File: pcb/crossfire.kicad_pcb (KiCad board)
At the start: 4 copper layers, 100 x 49.8 mm, 104 parts, among them J1 USB-C, J2 SWD+UART, J3 USB_A, J4 USB_A, J5 USB_A, J6 USB_A, SW1 BOOT, SW2 RESET, SW3 USER, U1 USBLC6-2SC6, U10 TPS2065C, U11 USBLC6-2SC6, U12 TPS2065C, U13 USBLC6-2SC6, U2 W25Q128JVS, U3 RP2350A, U4 AP63203WU, U5 USB2514B, U6 TPS2065C, U7 USBLC6-2SC6, U8 TPS2065C, U9 USBLC6-2SC6, Y1 12MHz, Y2 24MHz

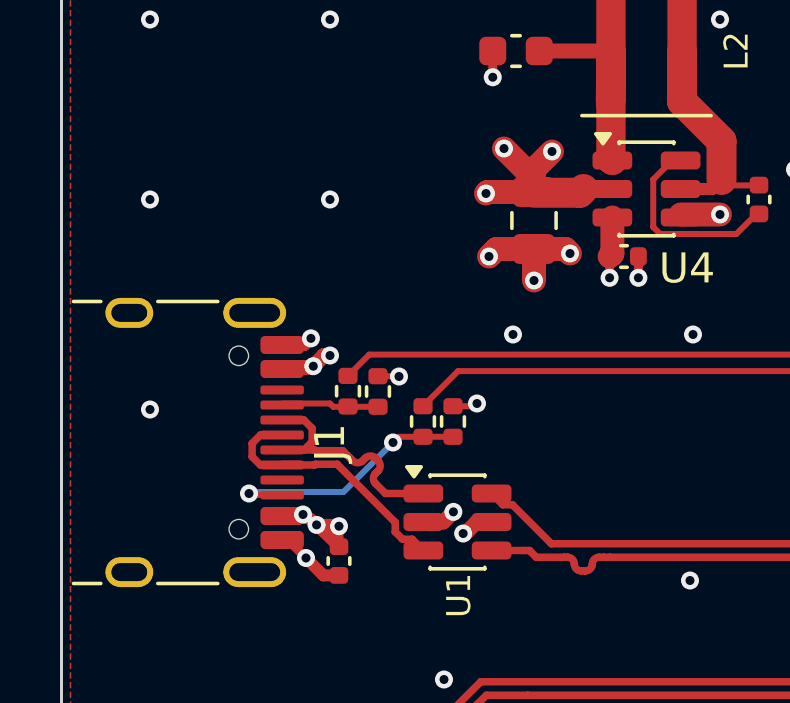
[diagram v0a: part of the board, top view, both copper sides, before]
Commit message: a resettable fuse on the 5 V input
F1, a 1812 polymer fuse with a 2.6 A hold and a 5 A trip, goes in series with VBUS at the
receptacle, ahead of everything. The wire between the receptacle's four VBUS pins and the fuse is
its own net, VBUS_IN, in the heavy-copper class; everything after the fuse is +5V as before. On the
board the fuse sits 5 mm from the receptacle in a spot checked clear of every other net's copper,
with its pads on the two nets and the receptacle's VBUS pads moved to the new one. The copper from
those pads through the fuse to the 5 V vias is the next hand edit; until it is drawn the rules
check lists the old VBUS tracks as shorting the two nets. The design document says why a
resettable part and what it costs.

Co-Authored-By: Claude Fable 5.1 <noreply@anthropic.com>
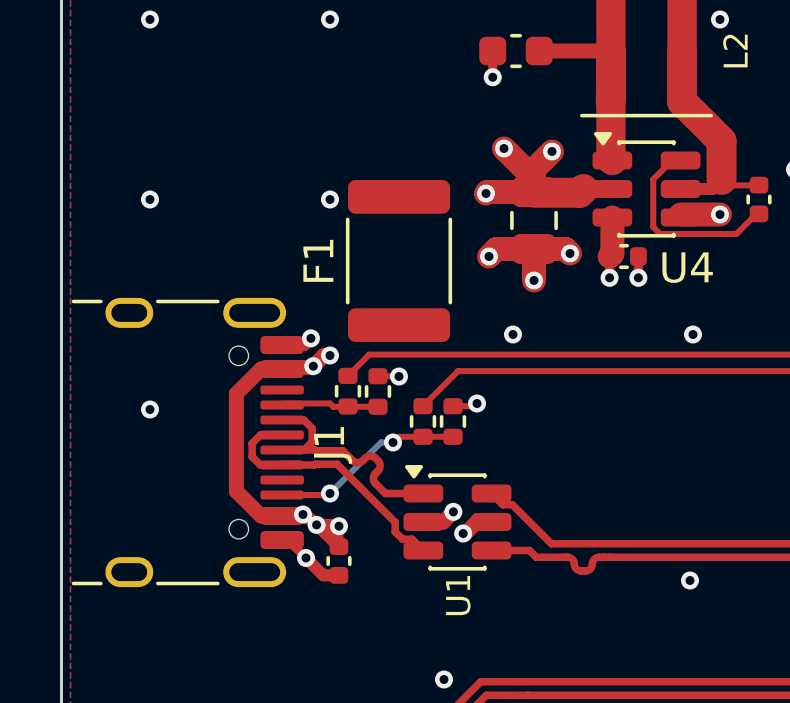
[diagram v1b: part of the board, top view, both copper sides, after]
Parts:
- added F1: 2.6A, Fuse:Fuse_1812_4532Metric, F.Cu at (109.8, 62.0)
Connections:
- J1 pad A4: +5V -> /upstream_data/VBUS_IN
- J1 pad A9: +5V -> /upstream_data/VBUS_IN
- J1 pad B4: +5V -> /upstream_data/VBUS_IN
- J1 pad B9: +5V -> /upstream_data/VBUS_IN
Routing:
- net +5V: track 34.7 -> 41.6 mm
- net /upstream_data/CC2: track 8.71 -> 6.50 mm

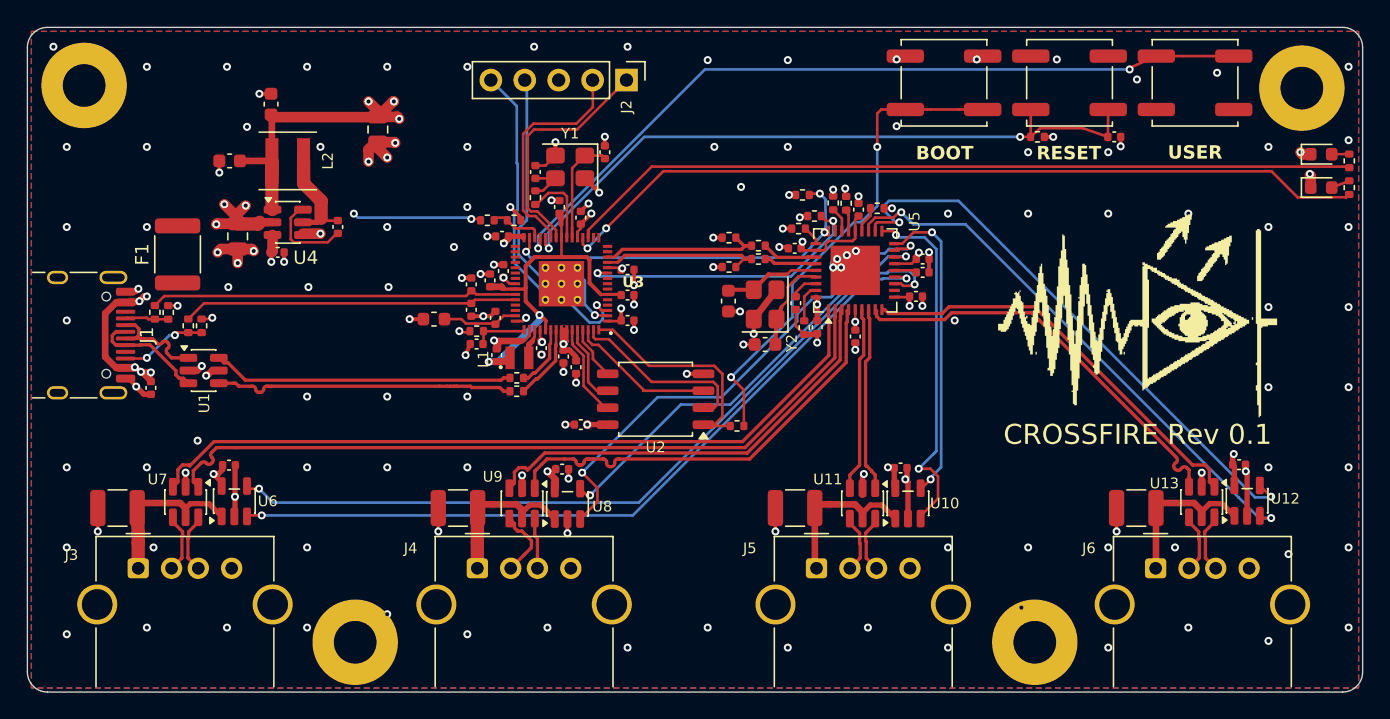
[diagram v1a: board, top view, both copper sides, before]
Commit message: board: VBUS routed through the fuse; the export names the fuse's package plainly
The receptacle's VBUS pads reach the fuse on their own net and the fuse feeds the 5 V plane; the
rules check is clean with parity and a fresh fill. The bill's footprint column now reduces a fuse
footprint's two-size name to its imperial code, as it already did for the chip parts, so the
fabricator's parser reads 1812 and not the metric 4532.

Co-Authored-By: Claude Fable 5.1 <noreply@anthropic.com>
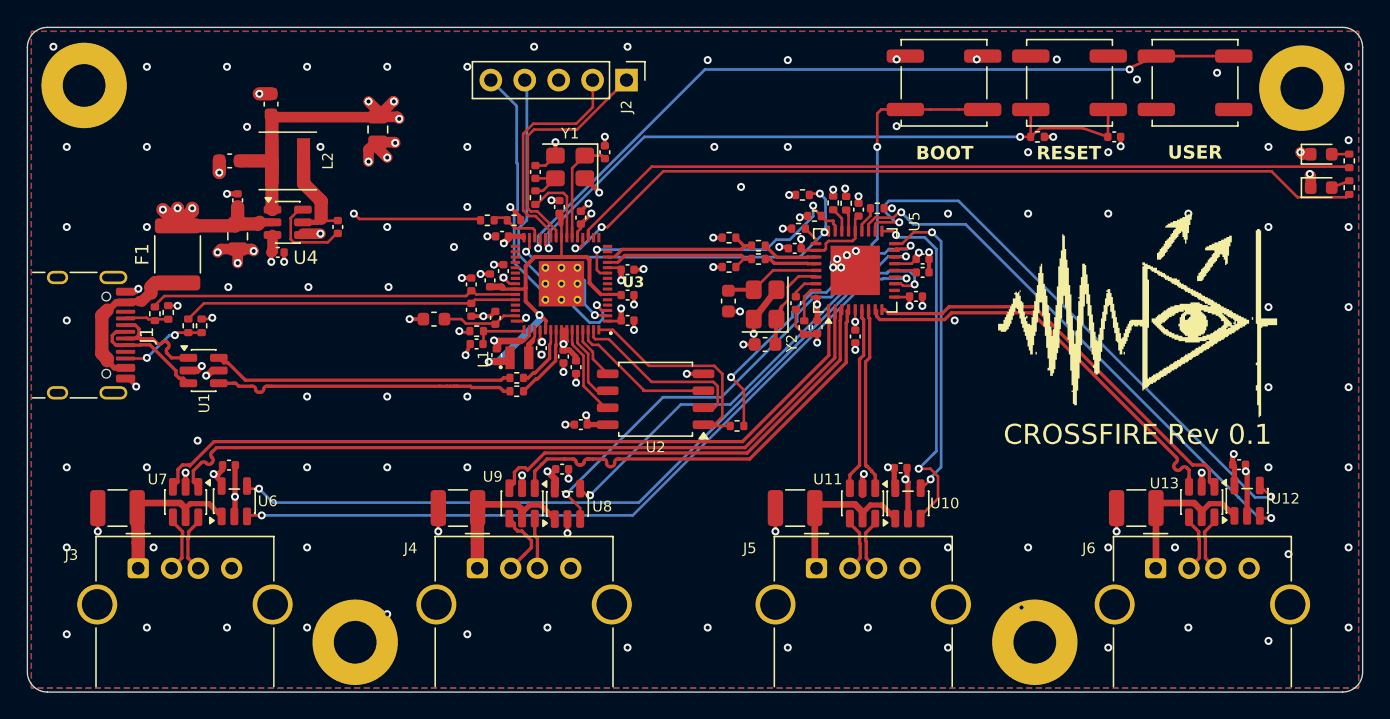
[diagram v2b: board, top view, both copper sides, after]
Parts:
- moved C1 15.5 mm to (114.2, 58.0), turned to -90 degrees
- moved R3 0.11 mm to (108.0, 66.5)
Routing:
- net /upstream_data/VBUS_IN: track 0.00 -> 11.6 mm
- net +5V: track 41.6 -> 35.0 mm, vias 16 -> 10
- net +3V3: track 59.6 -> 61.8 mm
- net Net-(U3-GPIO15): track 61.3 -> 62.4 mm
- net GND: track 88.6 -> 87.6 mm, vias 160 -> 161
- net /HUB_RESET: track 22.7 -> 23.4 mm

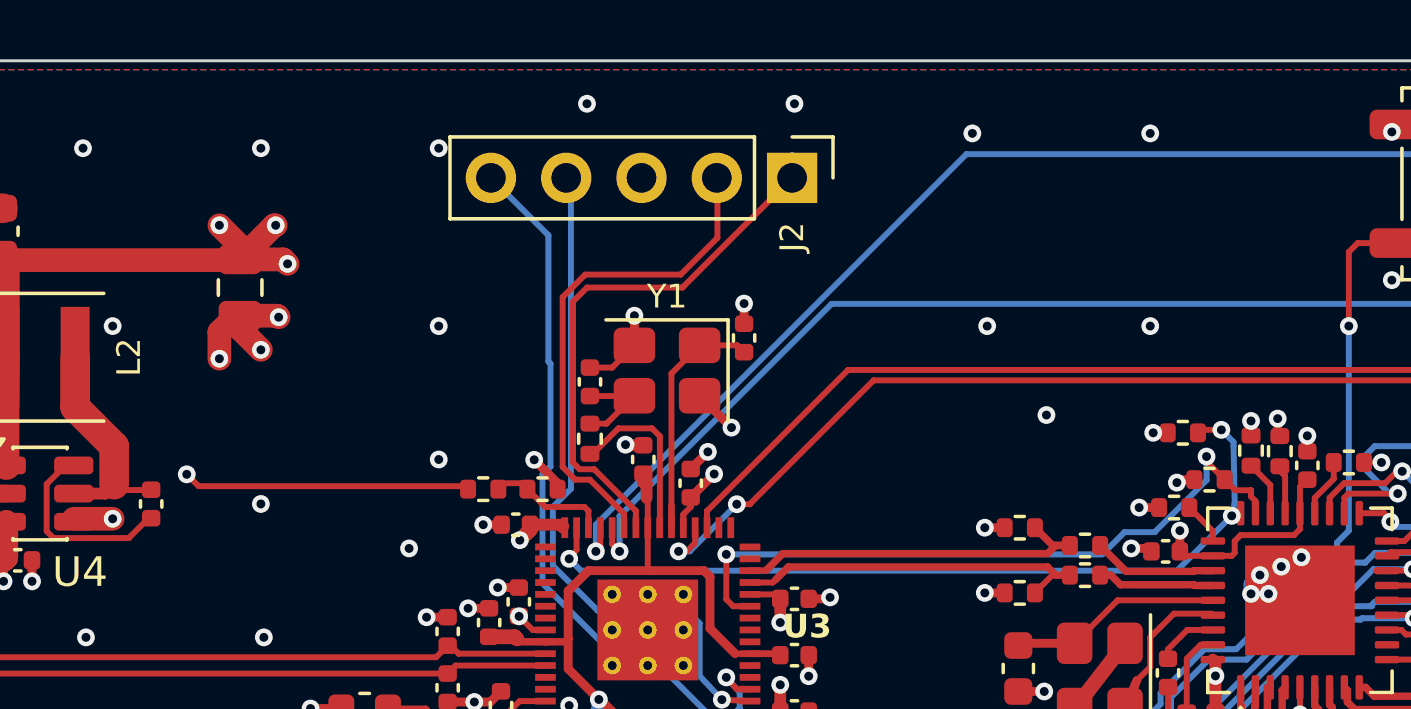
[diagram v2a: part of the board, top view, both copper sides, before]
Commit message: review: an indicator that lights, test points, and the sense divider gone
The green indicator could not have lit: a 3.1 V part on 3.3 V through 1 k leaves a fifth of a
milliamp. It becomes a 2.1 V yellow-green (LITEON LTST-C194KGKT, C913102) and both indicators
run through 330 ohm (C25104), about 4 mA each.

The VBUS sense divider watched the one rail the board runs from and could only ever read high.
Its two resistors, their ground, the wires, the hierarchical label and the sheet pins on both
sides are gone, GPIO17 carries a no-connect, and on the board the parts, their tracks, the
divider's 0.2 mm feed and the one via it left dangling are removed.

Eight test points go on the mcu sheet -- the PIO host pair, the processor's own USB pair, the
three rails and ground -- as bare 1 mm pads that the library keeps out of the bill and the
placement file. On the board they are parked in two rows in the open strip along the back edge,
references hidden, for the hand to place where a probe wants them; the seven connections to draw
are what the rules check lists.

Co-Authored-By: Claude Fable 5.1 <noreply@anthropic.com>
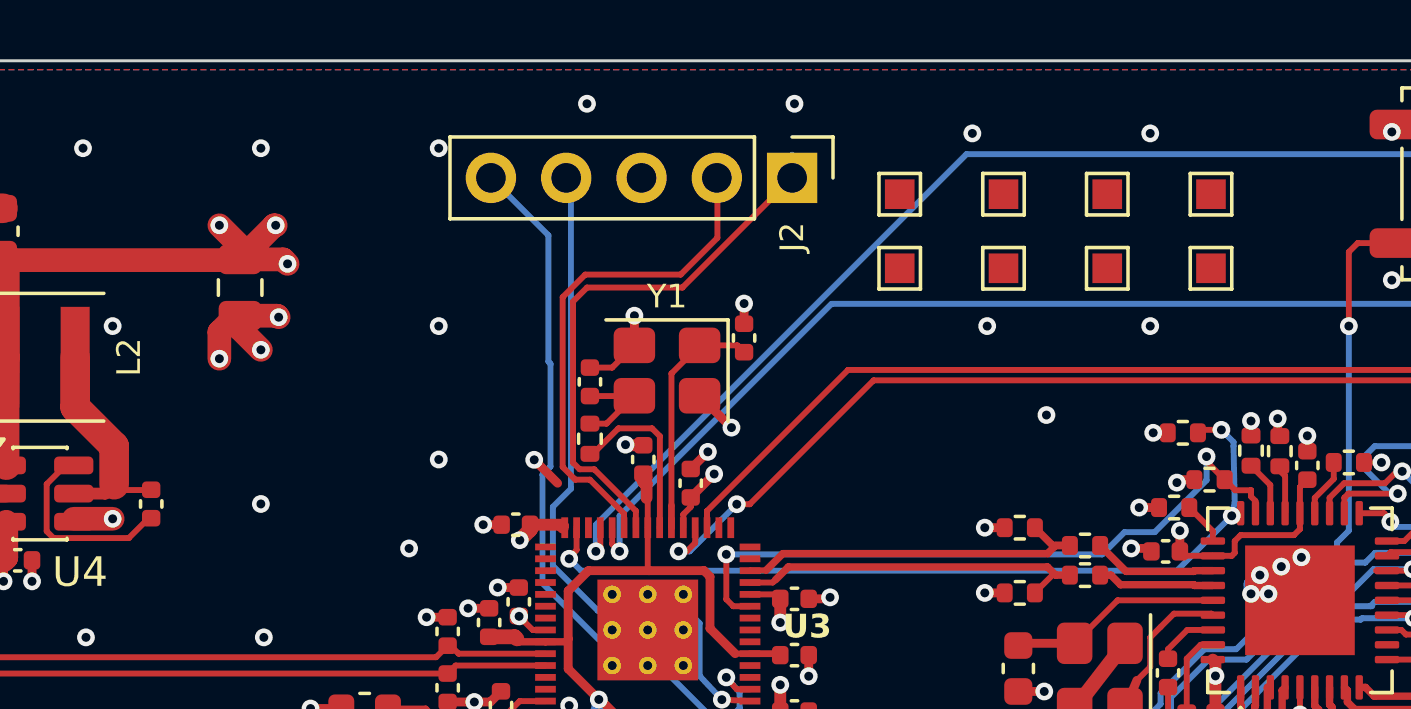
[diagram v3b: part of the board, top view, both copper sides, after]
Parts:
- removed R5, R6: 100k, Resistor_SMD:R_0402_1005Metric
- added TP1: TestPoint, TestPoint:TestPoint_Pad_1.0x1.0mm, F.Cu at (147.0, 49.5)
- added TP2: TestPoint, TestPoint:TestPoint_Pad_1.0x1.0mm, F.Cu at (150.5, 49.5)
- added TP3: TestPoint, TestPoint:TestPoint_Pad_1.0x1.0mm, F.Cu at (154.0, 49.5)
- added TP4: TestPoint, TestPoint:TestPoint_Pad_1.0x1.0mm, F.Cu at (157.5, 49.5)
- added TP5: TestPoint, TestPoint:TestPoint_Pad_1.0x1.0mm, F.Cu at (147.0, 52.0)
- added TP6: TestPoint, TestPoint:TestPoint_Pad_1.0x1.0mm, F.Cu at (150.5, 52.0)
- added TP7: TestPoint, TestPoint:TestPoint_Pad_1.0x1.0mm, F.Cu at (154.0, 52.0)
- added TP8: TestPoint, TestPoint:TestPoint_Pad_1.0x1.0mm, F.Cu at (157.5, 52.0)
- D1: value green -> yellow-green
- R10, R11: value 1k -> 330R
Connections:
- U3 pad 28: /VBUS_DET -> unconnected-(U3-GPIO17-Pad28)
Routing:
- net +5V: track 35.0 -> 25.3 mm, vias 10 -> 9
- net /VBUS_DET: track 3.91 -> 0.00 mm

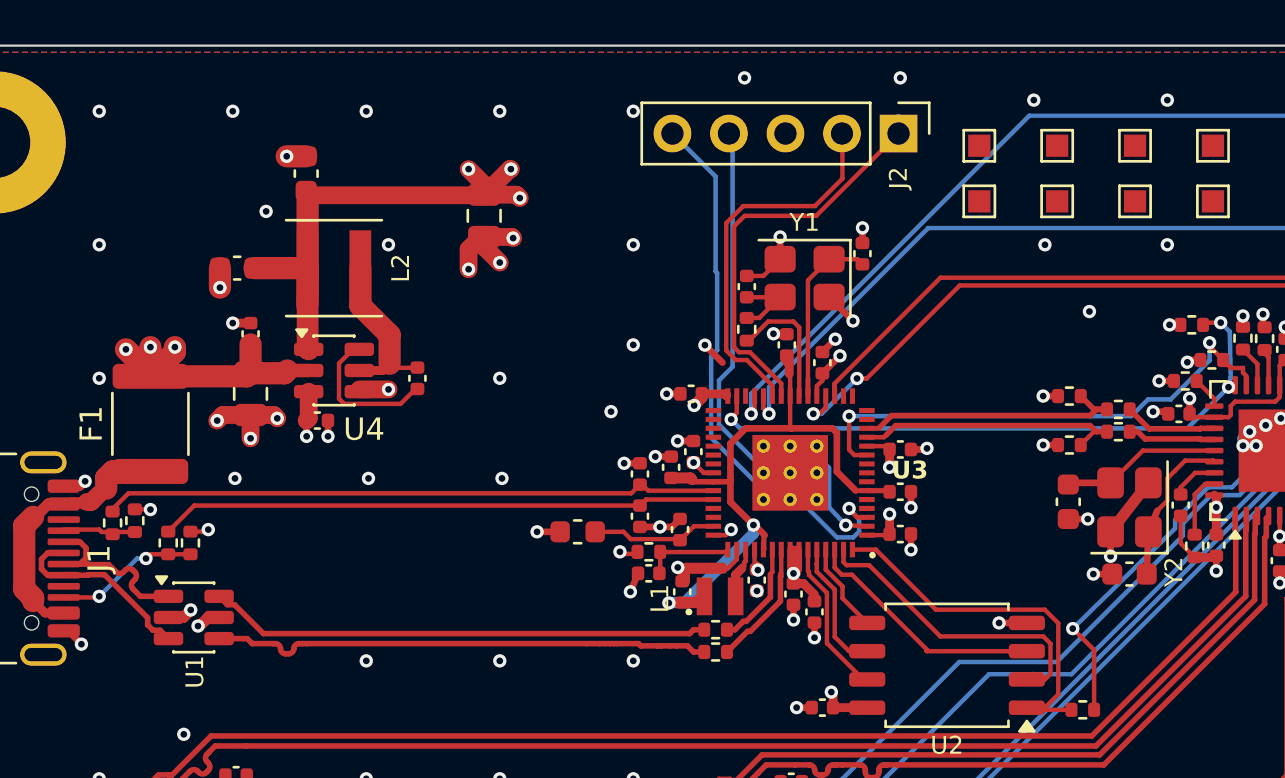
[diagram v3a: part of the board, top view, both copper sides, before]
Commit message: C44 comes out: the sixth IOVDD pin shares the regulator's input capacitor
There is no room at that pin for a capacitor of its own, the 4.7 uF on VREG_VIN sits 2.5 mm from
it on the same net, and the vendor's own board shares a capacitor between two pins in exactly
that situation. The capacitor, its wires and junction leave the sheet; the footprint, its stub,
its via and the segment the stub left behind leave the board. The design document records the
reversal next to the addition.

Co-Authored-By: Claude Fable 5.1 <noreply@anthropic.com>
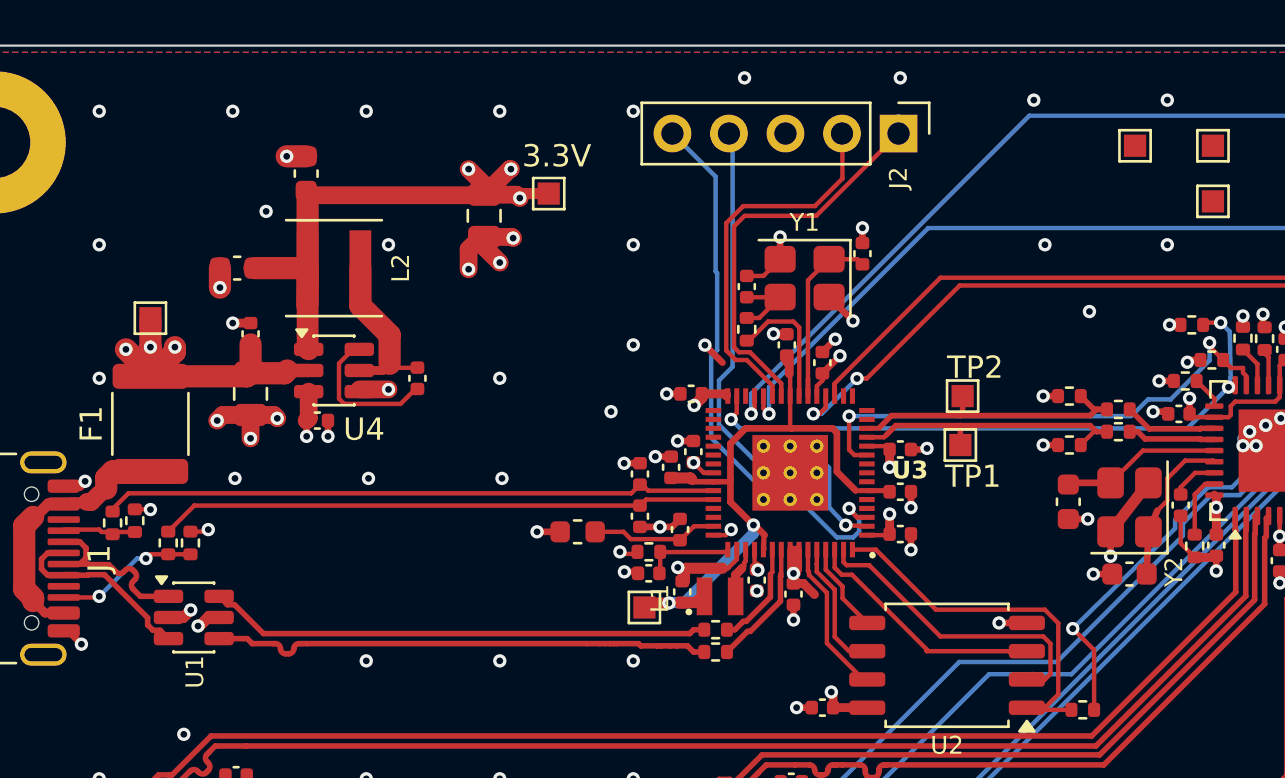
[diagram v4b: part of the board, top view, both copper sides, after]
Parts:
- removed C44: 100n, Capacitor_SMD:C_0402_1005Metric
- moved TP5 37.6 mm to (109.8, 57.2)
- moved TP7 28.6 mm to (131.9, 70.2)
- moved TP6 22.9 mm to (127.7, 51.6)
- moved TP1 13.5 mm to (146.2, 63.0)
- moved TP2 12.0 mm to (146.2, 60.8)
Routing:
- net +3V3: track 61.8 -> 63.1 mm
- net +5V: track 25.3 -> 26.5 mm
- net +1V1: track 28.8 -> 29.9 mm
- net GND: track 87.6 -> 86.7 mm, vias 161 -> 160
- net /PIO_D-: track 12.6 -> 13.5 mm
- net /PIO_D+: track 12.6 -> 13.4 mm
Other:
- board text added: "3.3V"
- board text added: "TP1"
- board text added: "TP2"

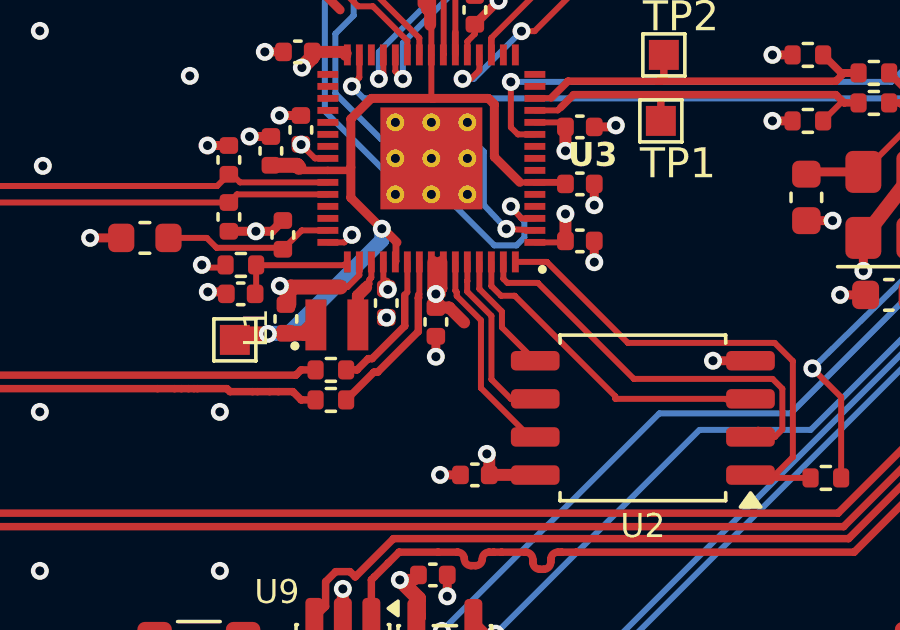
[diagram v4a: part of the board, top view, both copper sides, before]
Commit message: board: the segment C44's stub left behind
Co-Authored-By: Claude Fable 5.1 <noreply@anthropic.com>
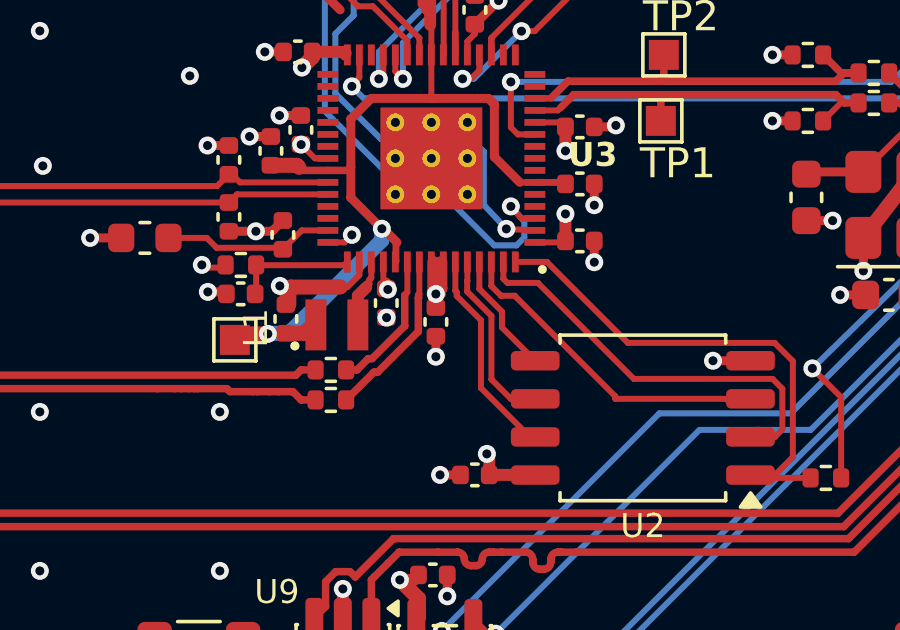
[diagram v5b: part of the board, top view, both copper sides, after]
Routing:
- net +3V3: track 63.1 -> 62.0 mm
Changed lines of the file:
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@@
-	)
-	(segment
-		(start 139.09267 69.17)
-		(end 138.65 69.17)
-		(width 0.4)
-		(layer "F.Cu")
-		(net "+3V3")
 	)
 	(segment
@@
 		(layer "F.Cu")
 		(net "+3V3")
-	)
-	(segment
-		(start 139.59267 69.67)
-		(end 139.09267 69.17)
-		(width 0.4)
-		(layer "F.Cu")
-		(net "+3V3")
